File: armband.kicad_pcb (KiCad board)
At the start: 6 copper layers, 48.8 x 40.1 mm, 86 parts, among them IC1 QSMP-1570, IC10 TLE493DW2B6A0HTSA1, IC2 BMI323, IC3 TPS259571DSGR, IC4 TPD6E001RSERG4, IC5 MP2722GRH-0000-Z, IC6 TPS62291DRVR, IC7 TPS62293DRVR, IC8 BQ27427YZFR, IC9 nRF52832-CIAA-G-R7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

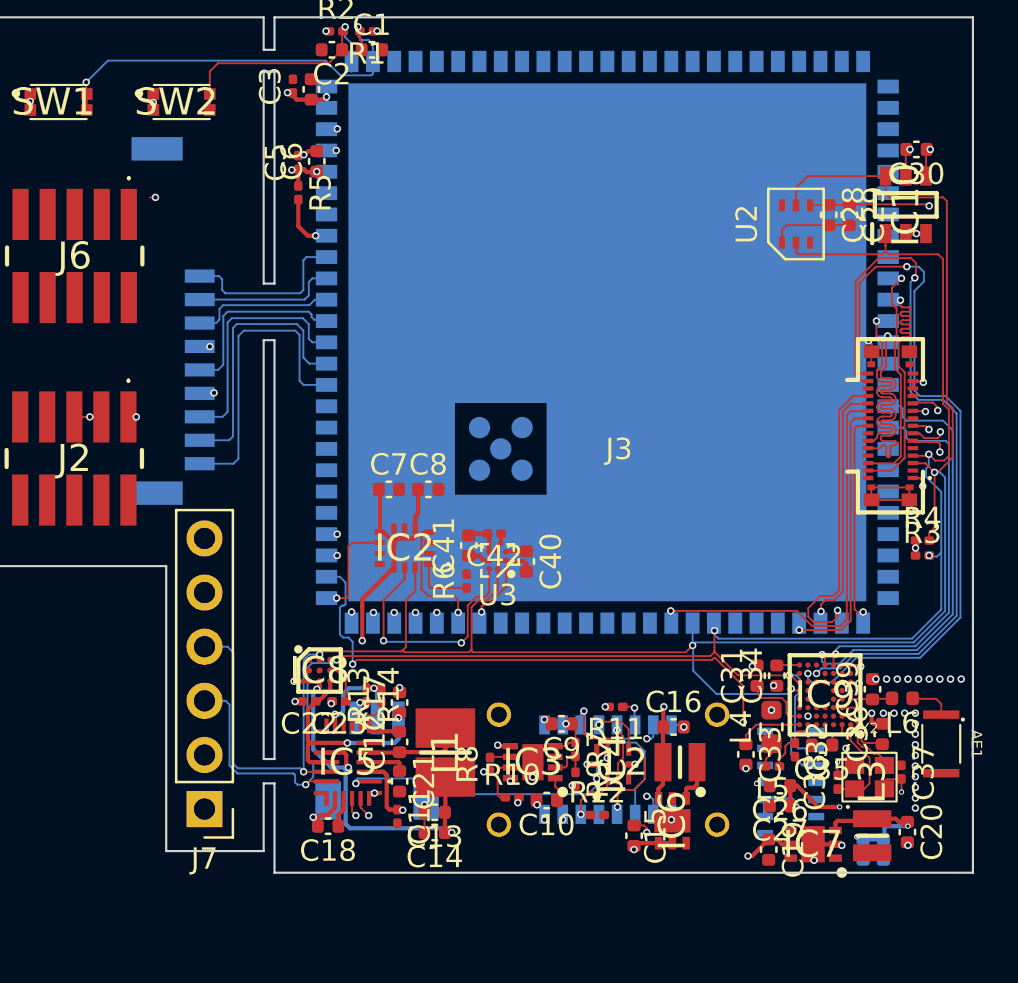
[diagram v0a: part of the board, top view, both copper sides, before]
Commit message: Reduce DRC findings
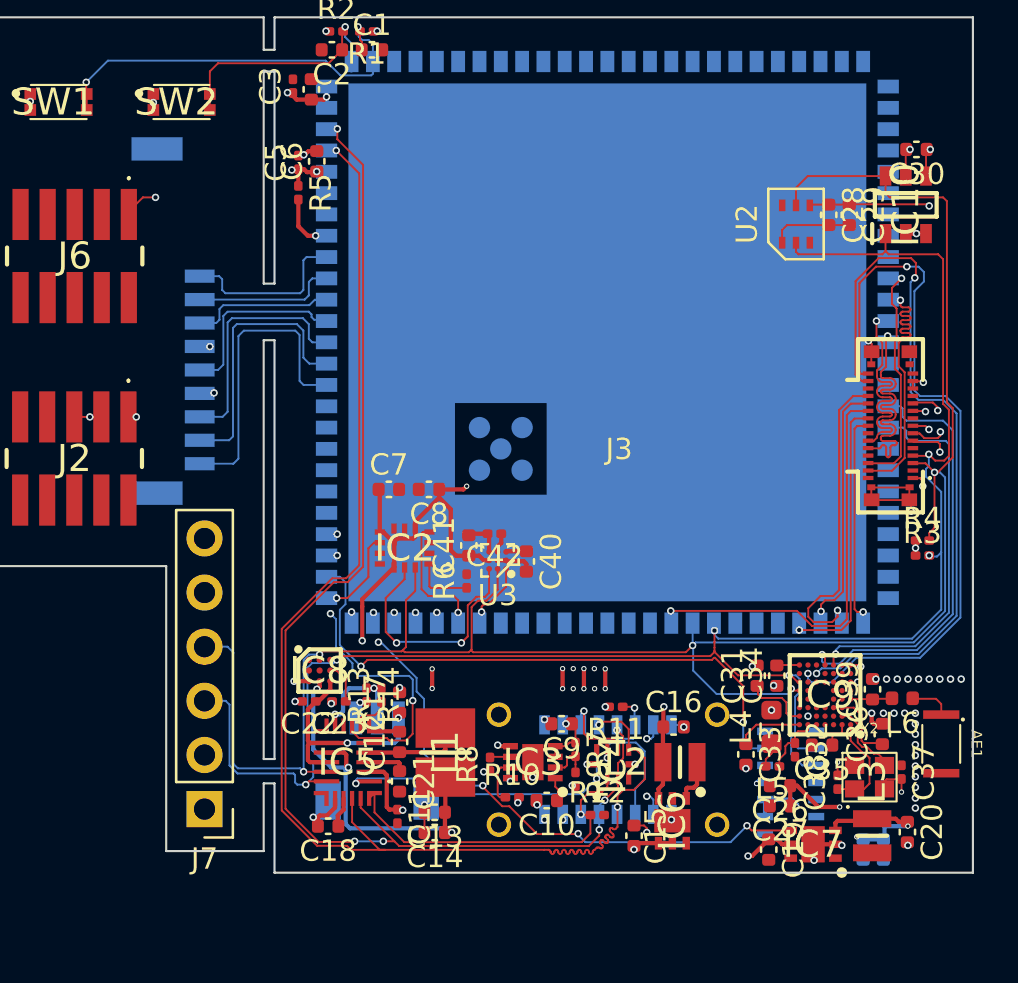
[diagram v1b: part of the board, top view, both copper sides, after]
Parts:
- turned C8 to 180 degrees
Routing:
- net QSMP_USB_DN: track 8.60 -> 64.8 mm, vias 4 -> 3
- net QSMP_USB_DP: track 4.49 -> 59.2 mm, vias 3 -> 6
- net +1V8: track 28.8 -> 81.4 mm, vias 5 -> 6
- net QSMP_BUCK_1V8_EN: track 0.50 -> 32.1 mm, vias 1 -> 5
- net MP2722_INT: track 0.50 -> 15.9 mm, vias 1 -> 3
- net Net-(IC4-IO2): track 3.46 -> 16.1 mm, vias 2 -> 1
- net +3V3: track 29.9 -> 35.0 mm, vias 16 -> 24
- net MAX_INT: track 31.7 -> 27.9 mm, vias 3 -> 2
- net Net-(IC4-IO1): track 18.8 -> 18.2 mm
- net BMI_INT2: track 4.95 -> 4.37 mm
- net GND: vias 58 -> 62
- added copper zone on In4.Cu, net +1V8

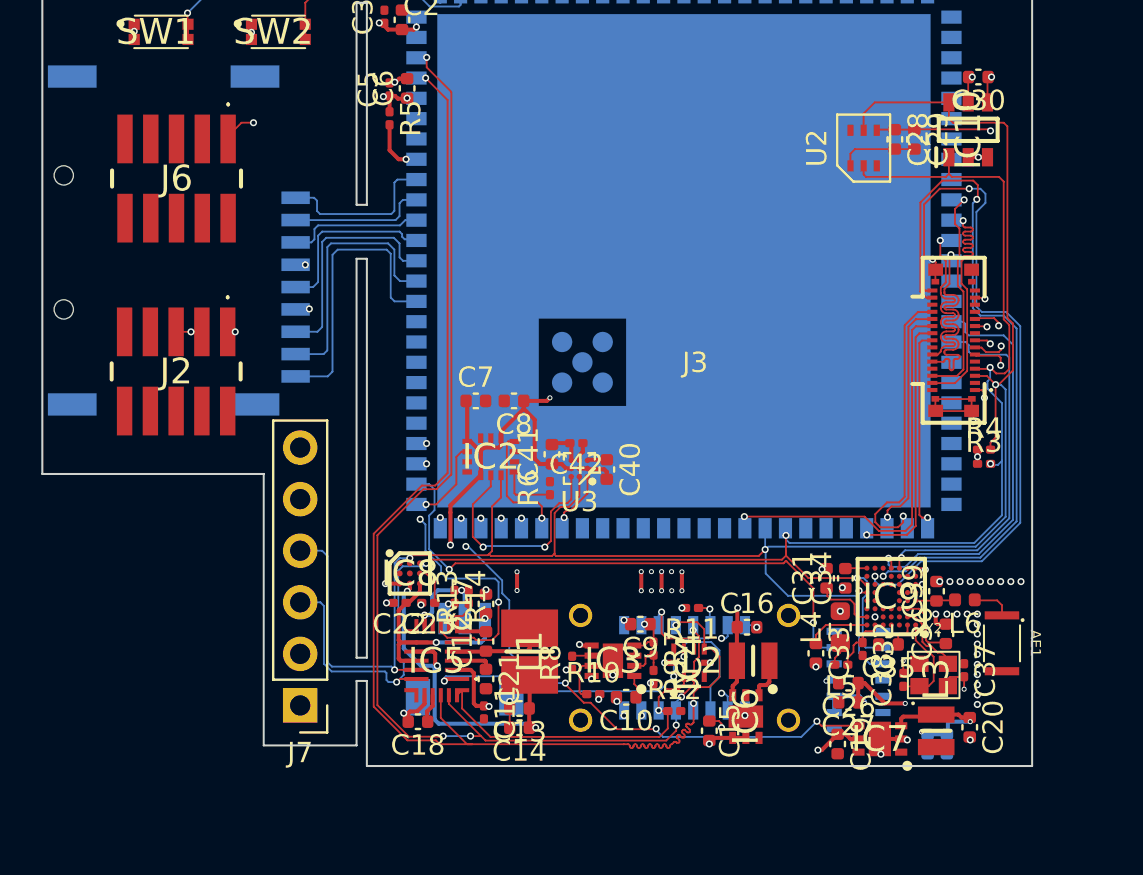
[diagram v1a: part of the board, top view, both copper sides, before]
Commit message: Add debug connections
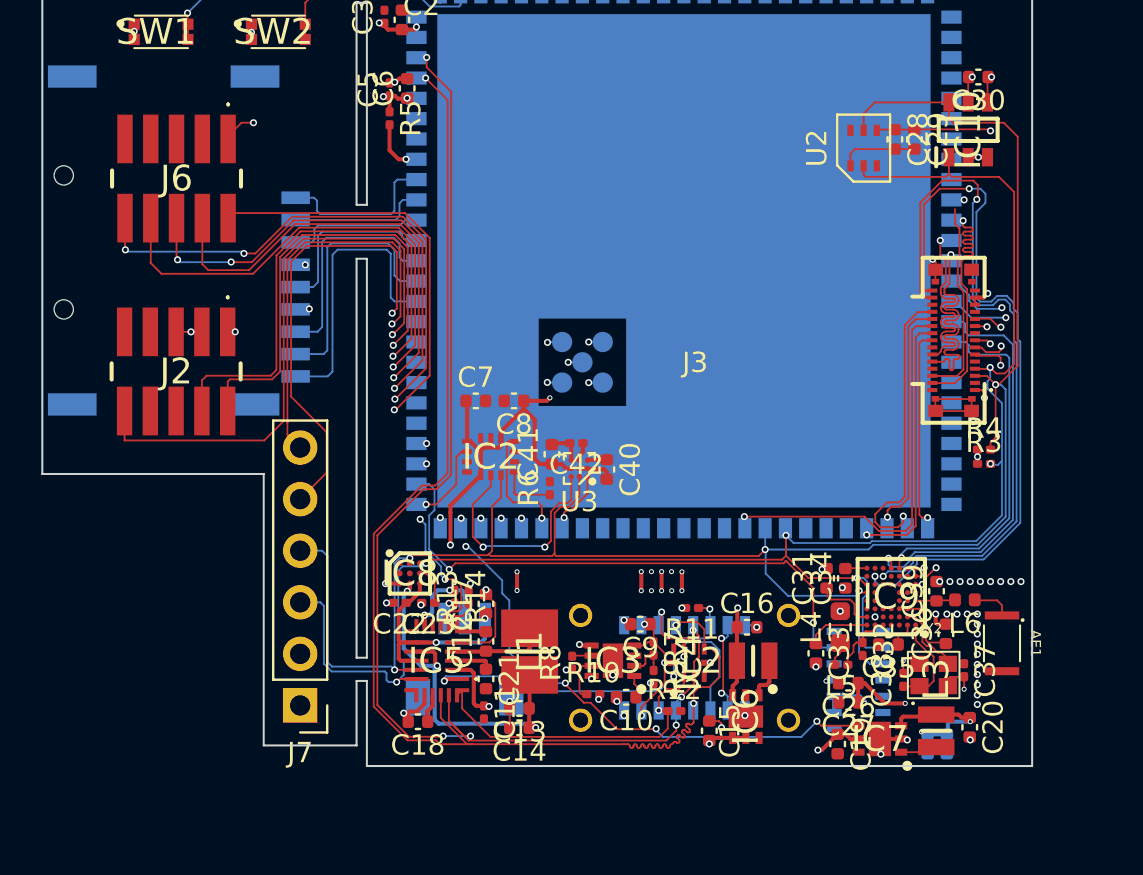
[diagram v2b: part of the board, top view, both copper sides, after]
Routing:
- net NRF_NRST: track 0.51 -> 67.7 mm, vias 1 -> 2
- net NRF_SWCLK: track 0.33 -> 63.8 mm, vias 1 -> 2
- net NRF_SWDIO: track 0.00 -> 62.9 mm, vias 0 -> 2
- net QSMP_RXD_DEBUG: track 0.00 -> 55.1 mm, vias 0 -> 2
- net QSMP_TXD_DEBUG: track 0.00 -> 53.0 mm, vias 0 -> 2
- net JTAG_NRST: track 0.00 -> 38.6 mm, vias 0 -> 4
- net JTAG_TDI: track 0.00 -> 34.8 mm, vias 0 -> 2
- net JTAG_TDO: track 0.00 -> 34.2 mm, vias 0 -> 4
- net JTAG_TCK: track 0.00 -> 31.1 mm, vias 0 -> 2
- net JTAG_TMS: track 0.00 -> 31.0 mm, vias 0 -> 2
- net Net-(IC3-IN_1): track 6.83 -> 17.8 mm
- net MP2722_INT: track 15.9 -> 11.0 mm
- net GND: track 33.1 -> 37.4 mm
- net Net-(IC7-SW): track 0.00 -> 1.83 mm
- net QSMP_USB_DP: track 59.2 -> 60.5 mm
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
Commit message: Improve some connections
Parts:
- moved J2 1.05 mm to (116.6, 67.4)
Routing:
- net NRF_SWDIO: track 62.9 -> 61.6 mm
- net NRF_NRST: track 67.7 -> 66.4 mm
- net NRF_SWCLK: track 63.8 -> 62.5 mm
- net QSMP_DSI_D0P: track 10.4 -> 11.1 mm

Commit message: fixed drc errors
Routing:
- net JTAG_TMS: track 31.0 -> 34.6 mm
- net JTAG_NRST: track 38.9 -> 42.1 mm
- net JTAG_TDO: track 34.5 -> 37.2 mm
- net JTAG_TCK: track 31.2 -> 33.4 mm
- net JTAG_TDI: track 34.8 -> 36.7 mm
- net NRF_SWCLK: track 62.5 -> 64.1 mm
- net NRF_SWDIO: track 61.6 -> 62.7 mm
- net QSMP_BUCK_1V8_EN: track 32.1 -> 32.8 mm
- net NRF_NRST: track 66.4 -> 67.1 mm

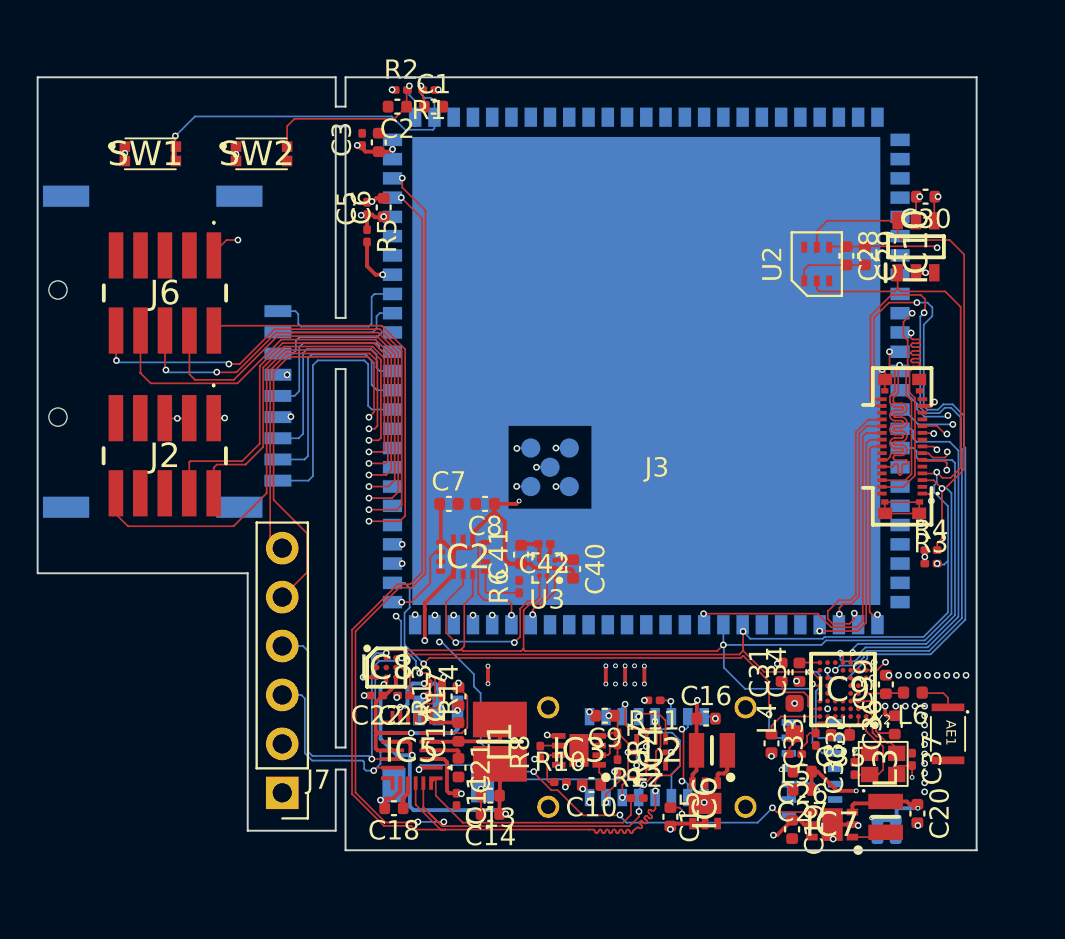
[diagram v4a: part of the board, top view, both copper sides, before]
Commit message: fixed drc errors
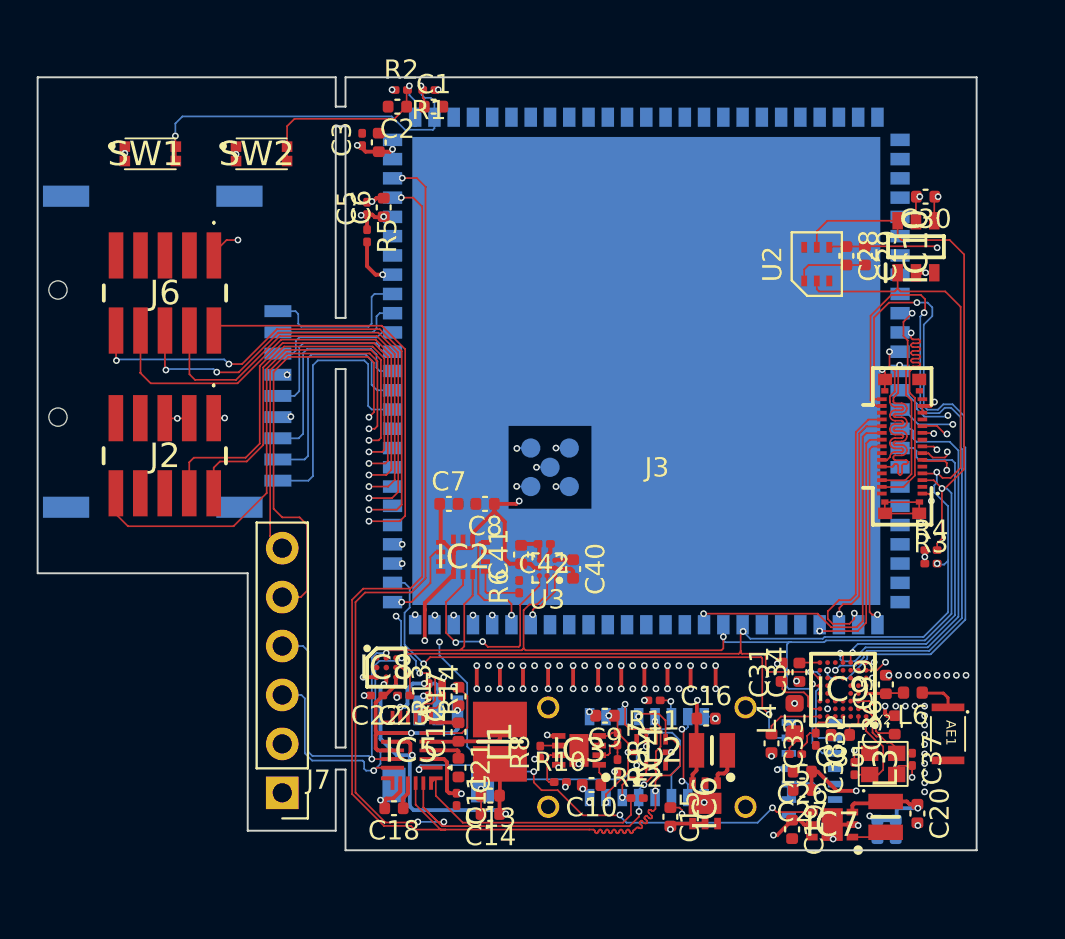
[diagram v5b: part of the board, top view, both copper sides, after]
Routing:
- net +3V3: track 35.2 -> 44.7 mm, vias 24 -> 38
- net QSMP_SDA: track 103.0 -> 100.8 mm
- net +1V8: track 82.2 -> 84.2 mm
- net QSMP_USB_DP: track 60.5 -> 62.0 mm
- net QSMP_USB_DN: track 64.8 -> 66.2 mm
- net QSMP_RXD_DEBUG: track 54.9 -> 56.0 mm
- net QSMP_BUCK_1V8_EN: track 32.8 -> 33.7 mm
- net QSMP_SCL: track 100.5 -> 101.2 mm
- net GND: track 37.4 -> 37.5 mm, vias 62 -> 78

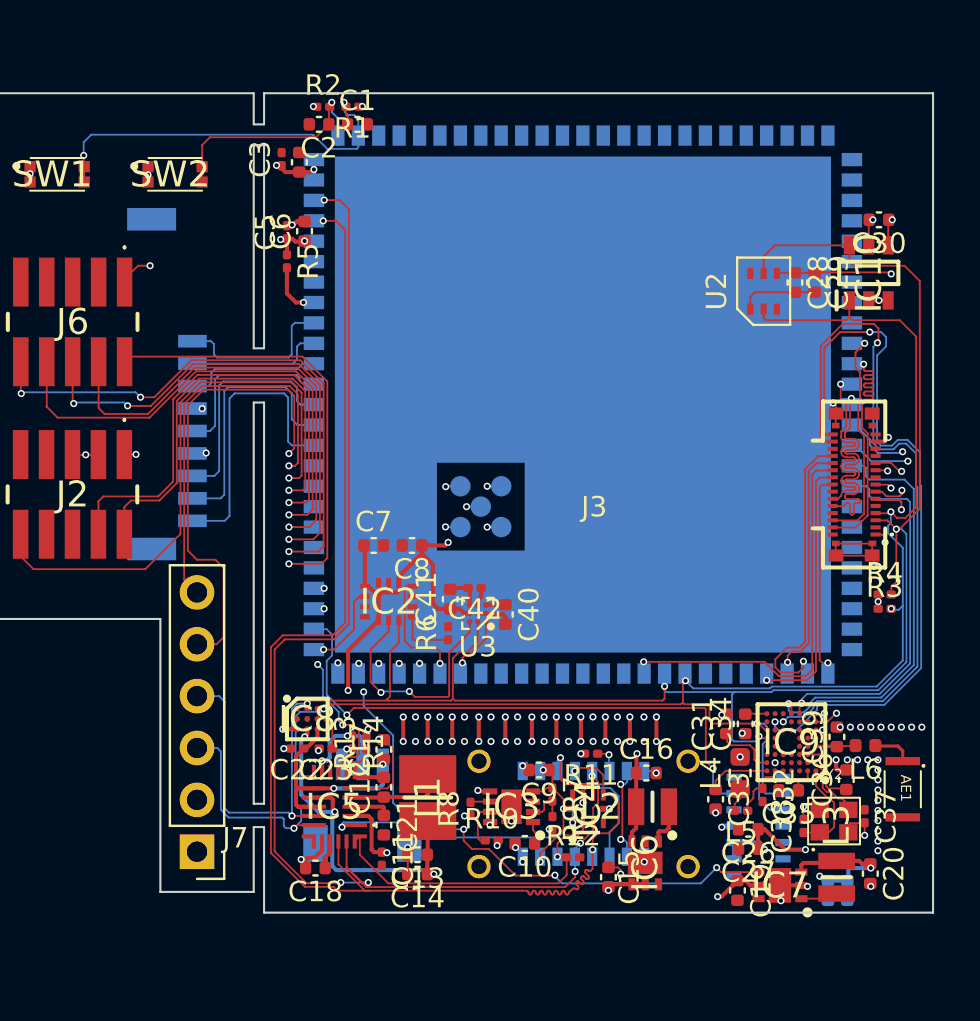
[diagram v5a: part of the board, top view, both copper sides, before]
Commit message: Update USB length matching
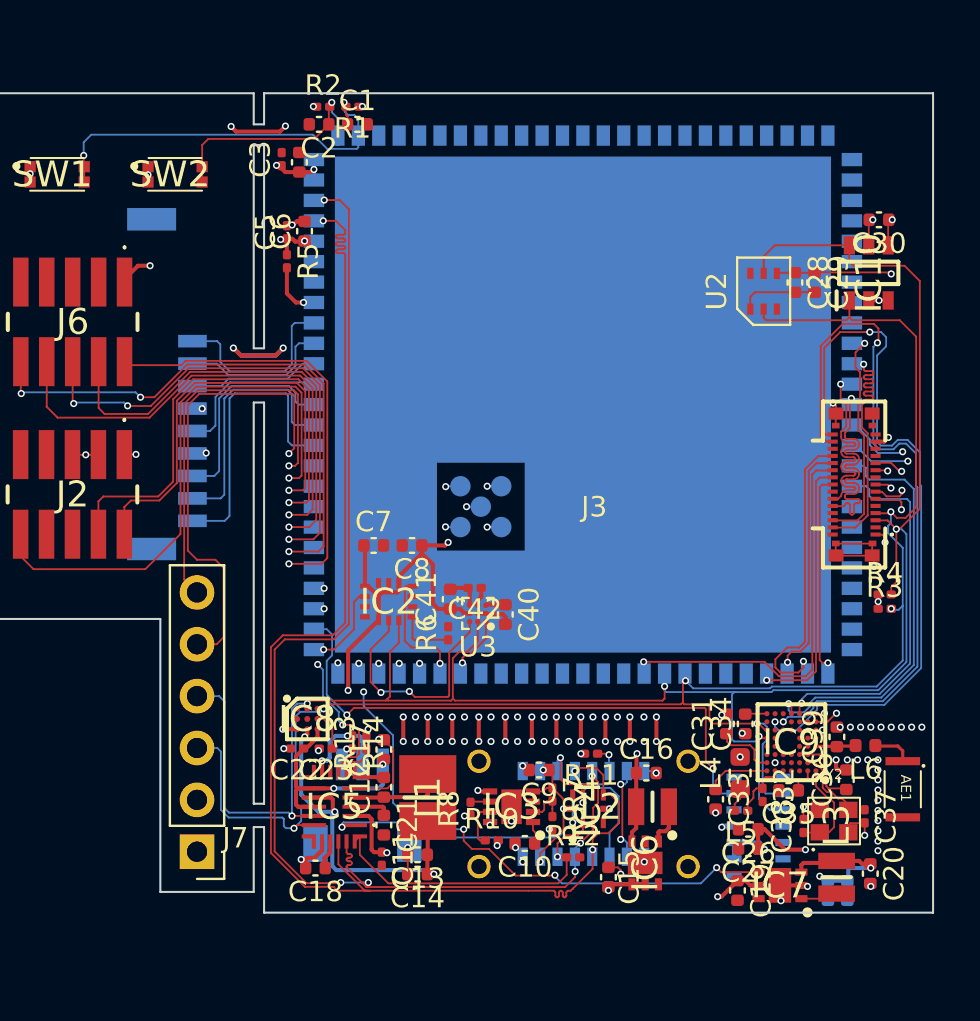
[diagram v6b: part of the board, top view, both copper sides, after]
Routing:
- net +3V3: track 44.7 -> 53.0 mm, vias 38 -> 42
- net SD_D2: track 8.10 -> 9.15 mm
- net SD_CLK: track 8.68 -> 7.79 mm
- net SD_D0: track 11.2 -> 10.5 mm
- net SD_D3: track 6.73 -> 7.37 mm
- net QSMP_USB_DN: track 66.2 -> 66.8 mm
